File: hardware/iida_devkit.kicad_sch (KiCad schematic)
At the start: 7 parts

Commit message: HW: Refactor the schematics
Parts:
- added R101, R102: 0 Ω, Resistor_SMD:R_1206_3216Metric, symbol Device:R
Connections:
- net GND: now also R101.2, R102.2; no longer H101.1, H102.1, H103.1, H104.1
- new net CHASSIS: H101.1, H102.1, H103.1, H104.1, R101.1, R102.1
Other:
- removed sheet Battery
- removed sheet USB
- sheet Microcontroller ports: added I2C, USB; removed I2C_SCL, I2C_SDA, USB_DN, USB_DP
- sheet Power ports: added BAT_MON_INTn, I2C, USB; removed V_5V0, V_BAT
- note added: "2. Power"
- note added: "3. Microcontroller"
- note added: "Block diagram"
- note added: "Description"
- note added: "Mechanical"
- note added: "Notes"
- note added: "Table of Contents"
- note removed: "2. USB"
- note removed: "3. Battery"
- note removed: "4. Power"
- note removed: "5. Microcontroller"
- moved on the sheet: FID101, FID102, FID103, H101, H102, H103, H104

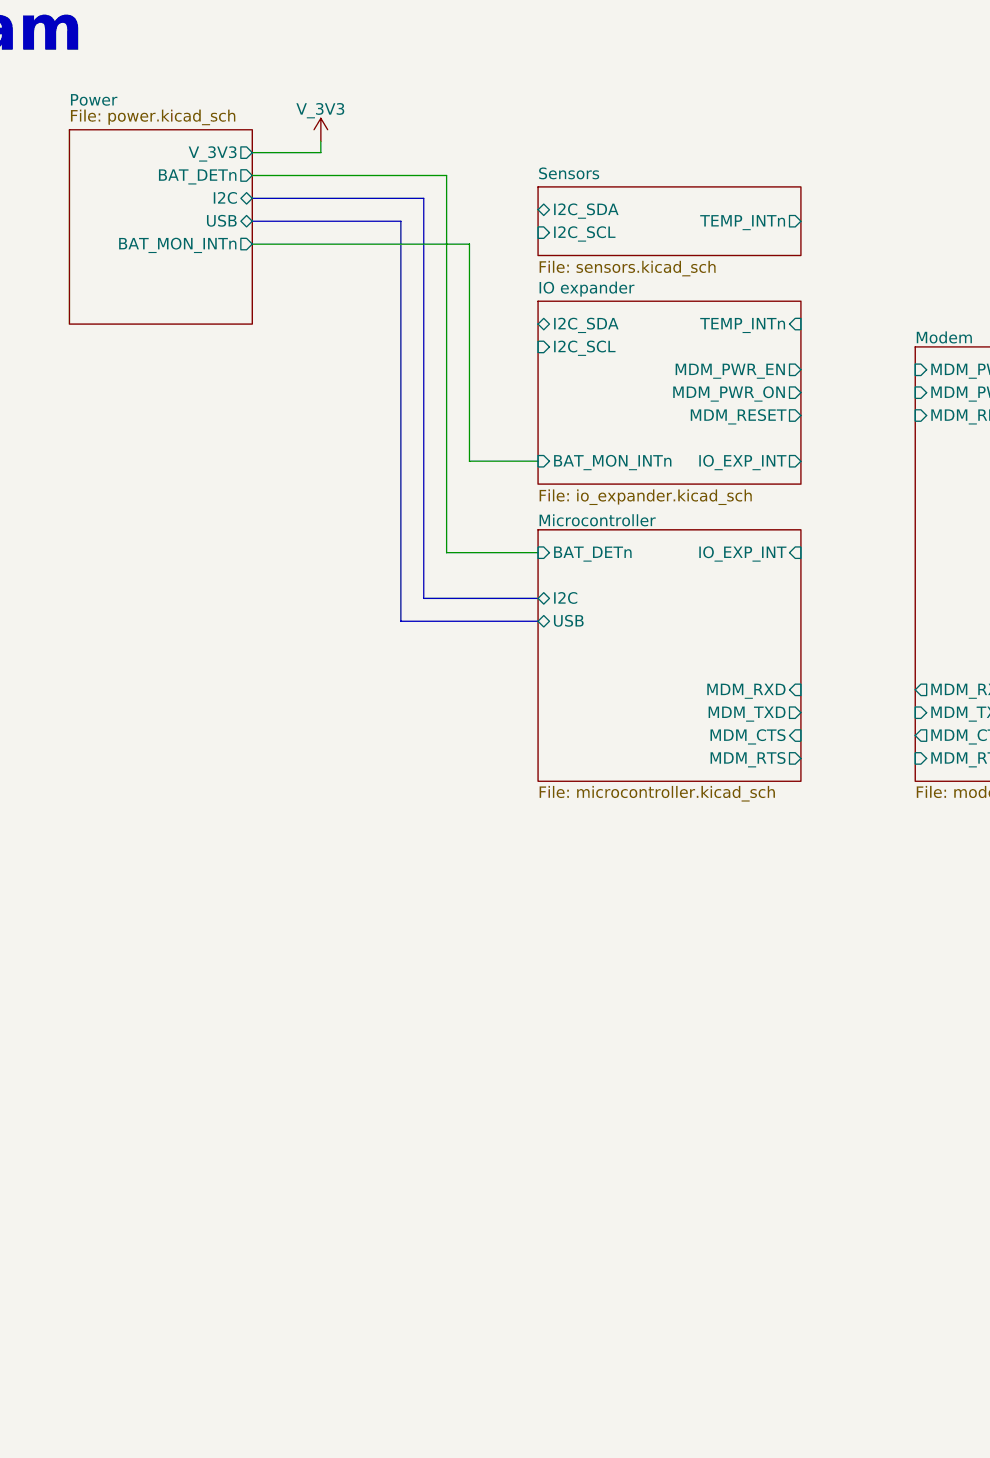
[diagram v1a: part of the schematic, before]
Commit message: Add EEPROM
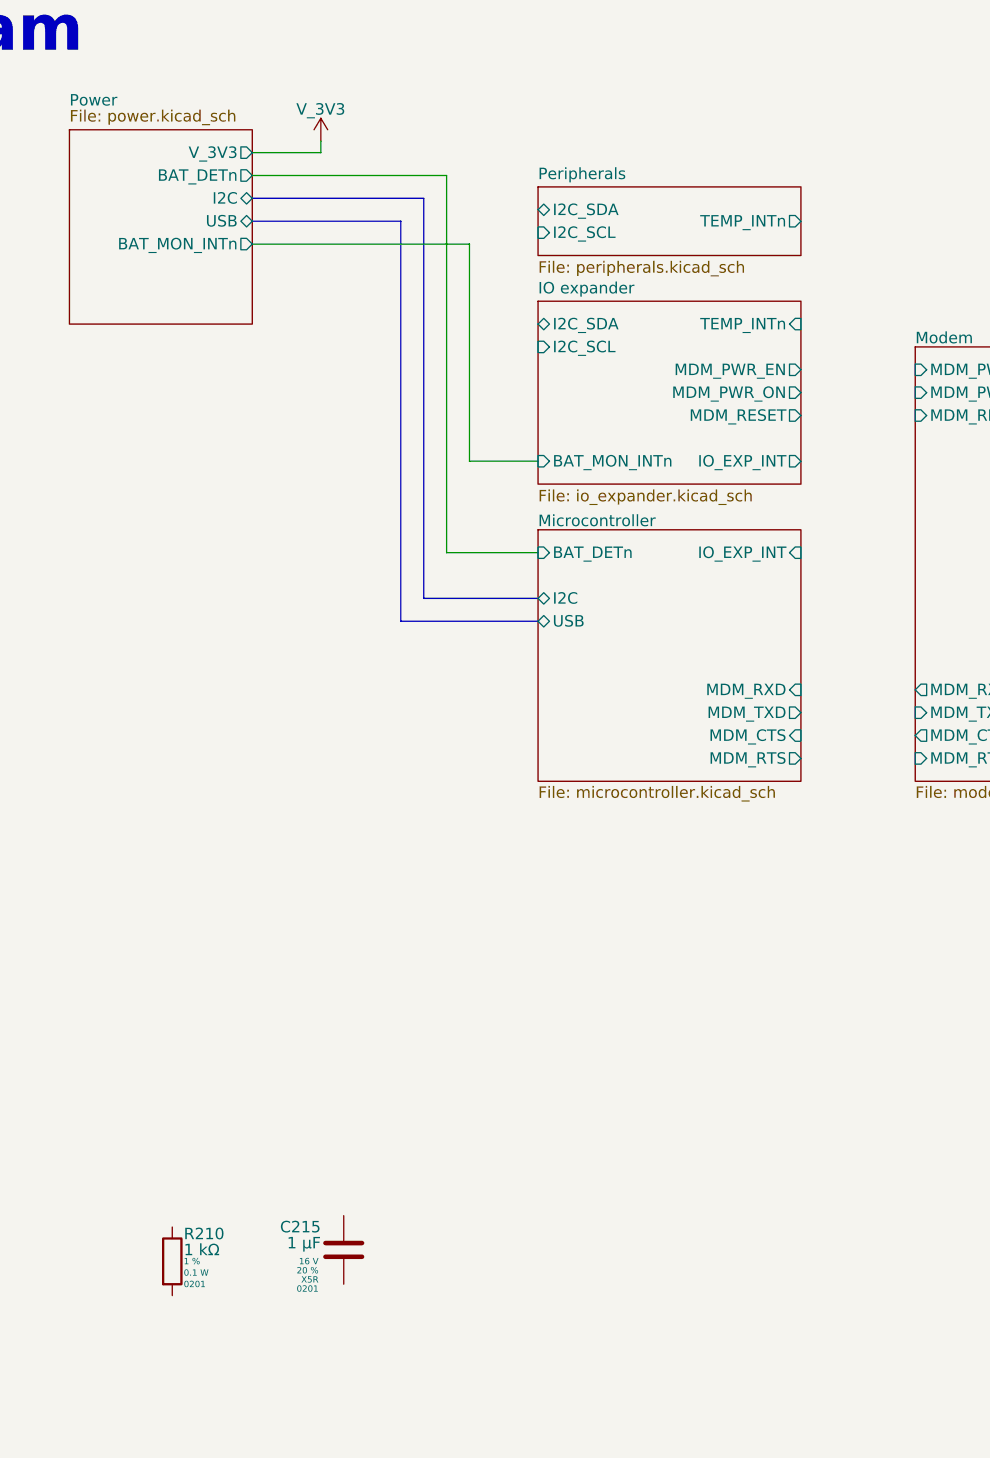
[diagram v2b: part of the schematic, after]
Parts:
- added C215: 1 µF, perfect_footprints:C_0201_0603Metric, symbol Device:C
- added R210: 1 kΩ, perfect_footprints:R_0201_0603Metric, symbol Device:R
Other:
- sheet Sensors renamed Peripherals
- sheet Peripherals: file sensors.kicad_sch -> peripherals.kicad_sch

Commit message: Refine schematics
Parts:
- removed C215: 1 µF, perfect_footprints:C_0201_0603Metric, symbol Device:C
- removed R210: 1 kΩ, perfect_footprints:R_0201_0603Metric, symbol Device:R
- renumbered FID101 to FID1, FID102 to FID2, FID103 to FID3, H101 to H1, H102 to H2, H103 to H3, H104 to H4, R102 to R1, R101 to R2
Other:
- removed sheet IO expander
- sheet Microcontroller ports: added EEPROM_WCn, {FLASH_QSPI}, {I2C}, {USB}; removed I2C, USB
- sheet Modem ports: added {SIM}; removed SIM_CLK, SIM_IO, SIM_RST
- sheet Peripherals ports: added BAT_MON_INTn, EEPROM_WCn, IO_EXP_INT, MDM_PWR_EN, MDM_PWR_ON, MDM_RESET, {FLASH_QSPI}, {I2C}; removed I2C_SCL, I2C_SDA, TEMP_INTn
- sheet Power ports: added {I2C}, {USB}; removed I2C, USB
- sheet SIM ports: added {SIM}; removed SIM_CLK, SIM_IO, SIM_RST
- note added: "4. Peripherals"
- note added: "5. Modem"
- note added: "6. SIM"
- note added: "7. Antennas"
- note removed: "10. Antennas"
- note removed: "6. Sensors"
- note removed: "7. IO expander"
- note removed: "8. Modem"
- note removed: "9. SIM"

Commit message: HW: Refine PDN
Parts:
- C1: renamed from R1; value 0 Ω -> 0.047 µF; footprint Resistor_SMD:R_1206_3216Metric -> Capacitor_SMD:C_1206_3216Metric; symbol Device:R -> Device:C; Digi-Key Part Number RMCF1206ZT0R00CT-ND -> (none); MPN RMCF1206ZT0R00 -> (none); Manufacturer Stackpole Electronics Inc -> (none); now not fitted; now left out of the parts list
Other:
- note added: "Place closely together."
- moved on the sheet: FID1, FID2, FID3, H1, H2, H3, H4, R2

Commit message: HW: Refine schematics
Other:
- sheet Microcontroller ports: added ST; removed BAT_DETn
- sheet Power ports: added ST; removed BAT_DETn
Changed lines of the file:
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@@
 			)
 		)
-		(pin "BAT_DETn" output
+		(pin "ST" output
 			(at 234.95 68.58 0)
 			(effects
@@
 			)
 		)
-		(pin "BAT_DETn" input
+		(pin "ST" input
 			(at 247.65 107.95 180)
 			(effects

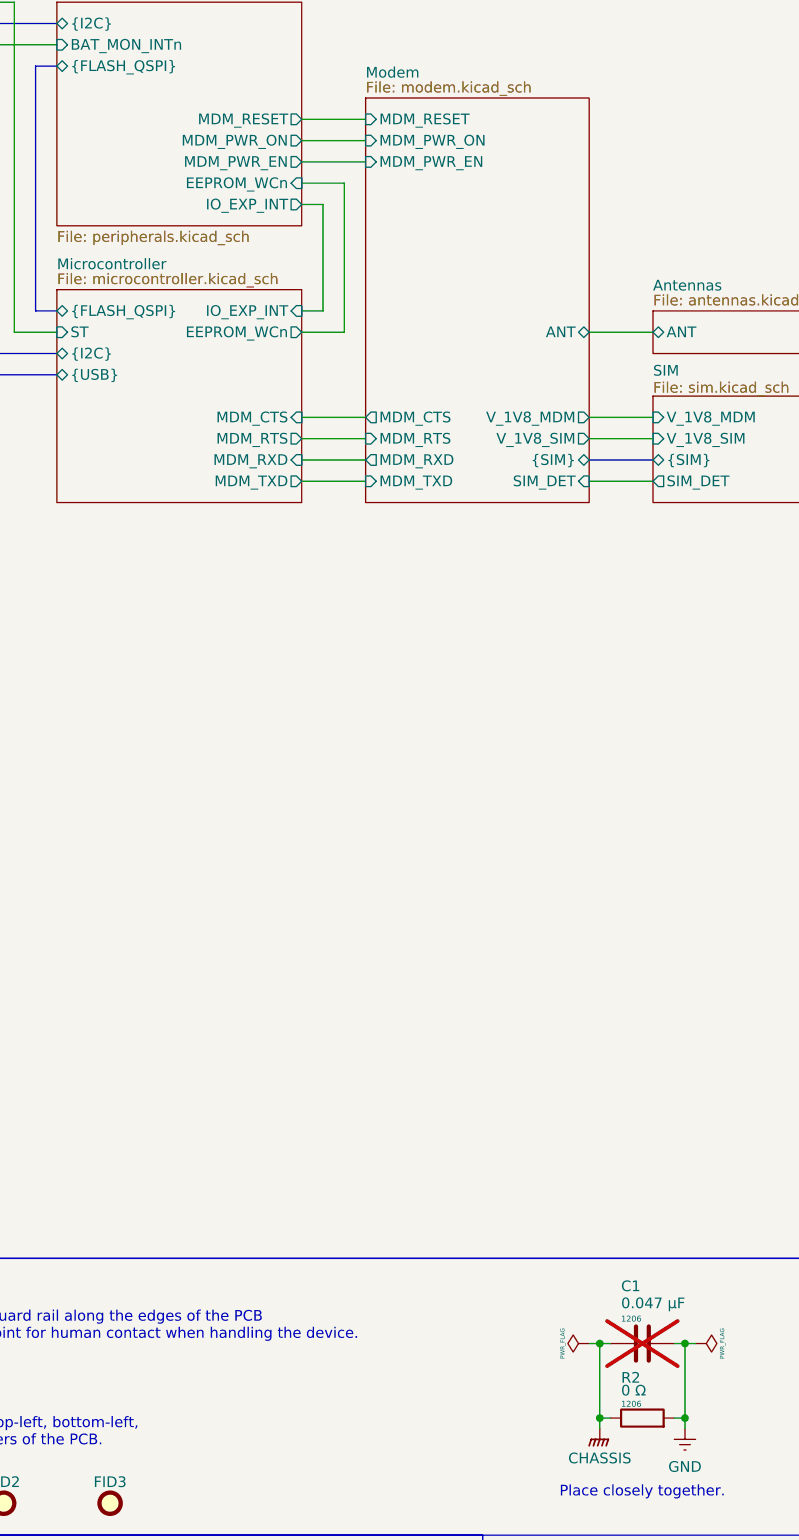
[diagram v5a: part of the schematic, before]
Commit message: HW: Redo MDM UART
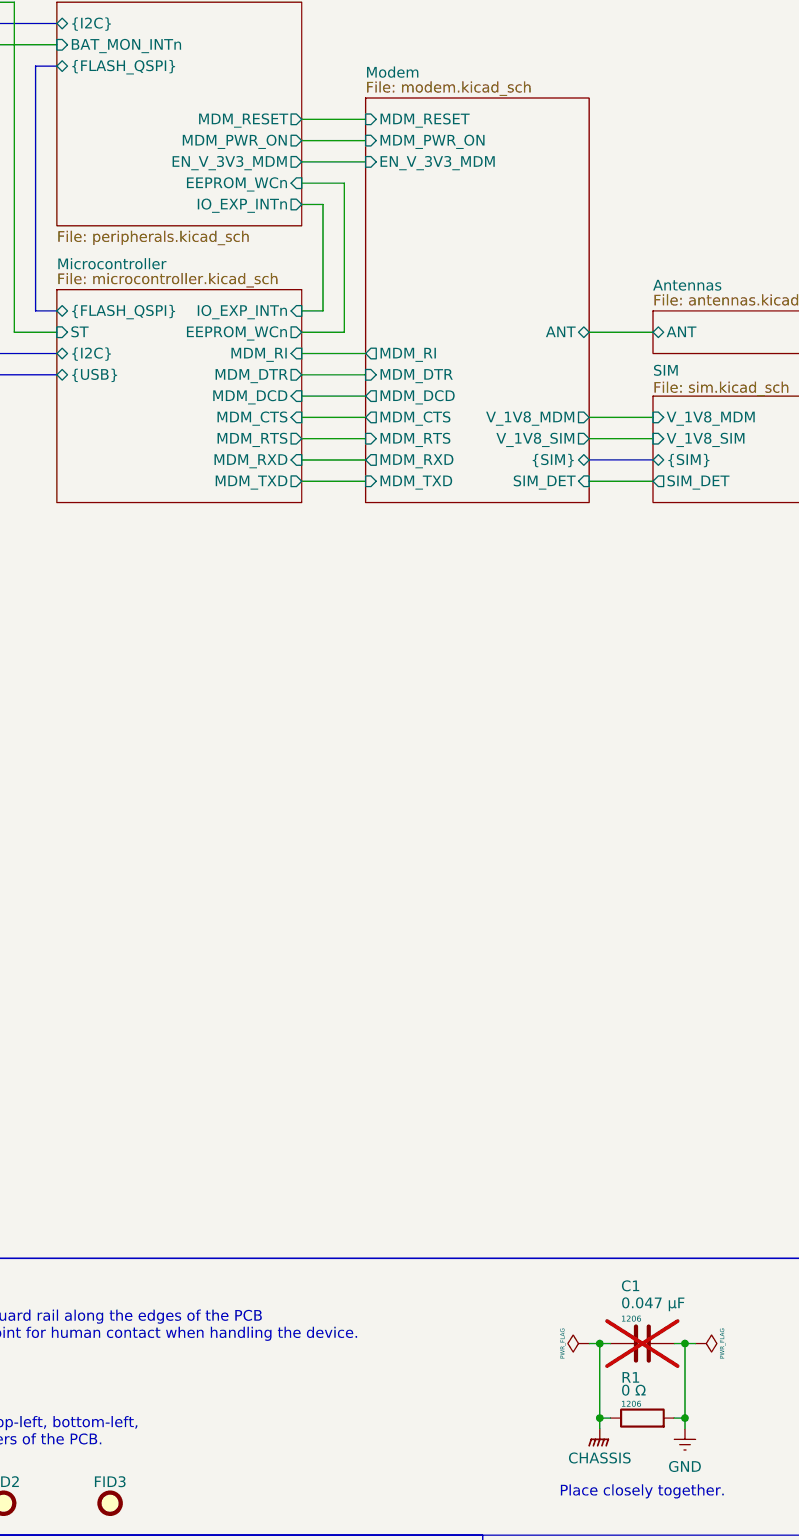
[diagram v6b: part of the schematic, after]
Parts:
- renumbered R2 to R1
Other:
- sheet Microcontroller ports: added IO_EXP_INTn, MDM_DCD, MDM_DTR, MDM_RI; removed IO_EXP_INT
- sheet Modem ports: added EN_V_3V3_MDM, MDM_DCD, MDM_DTR, MDM_RI; removed MDM_PWR_EN
- sheet Peripherals ports: added EN_V_3V3_MDM, IO_EXP_INTn; removed IO_EXP_INT, MDM_PWR_EN
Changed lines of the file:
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@@
+	(wire
+		(pts
+			(xy 276.86 110.49) (xy 284.48 110.49)
+		)
+		(stroke
+			(width 0)
+			(type default)
+		)
+	)
 	(wire
 		(pts
@@
 	(wire
 		(pts
+			(xy 276.86 115.57) (xy 284.48 115.57)
+		)
+		(stroke
+			(width 0)
+			(type default)
+		)
+	)
+	(wire
+		(pts
 			(xy 313.69 228.6) (xy 312.42 228.6)
 		)
@@
 		(pts
 			(xy 240.03 71.12) (xy 240.03 110.49)
+		)
+		(stroke
+			(width 0)
+			(type default)
+		)
+	)
+	(wire
+		(pts
+			(xy 276.86 113.03) (xy 284.48 113.03)
 		)
 		(stroke
@@
 		(in_pos_files yes)
 		(dnp no)
-		(property "Reference" "#PWR02"
+		(property "Reference" "#PWR04"
 			(at 322.58 245.11 0)
 			(hide yes)
@@
 			(project "iida_devkit"
 				(path "/b12a6e25-97fb-4aba-bc96-af8db389bb9a"
-					(reference "#PWR02")
+					(reference "#PWR04")
 					(unit 1)
 				)
@@
 		(in_pos_files yes)
 		(dnp no)
-		(property "Reference" "#PWR04"
+		(property "Reference" "#PWR02"
 			(at 242.57 68.58 0)
 			(hide yes)
@@
 			(project "iida_devkit"
 				(path "/b12a6e25-97fb-4aba-bc96-af8db389bb9a"
-					(reference "#PWR04")
+					(reference "#PWR02")
 					(unit 1)
 				)
@@
 		(in_pos_files yes)
 		(dnp no)
-		(property "Reference" "#PWR03"
+		(property "Reference" "#PWR01"
 			(at 187.96 250.19 0)
 			(hide yes)
@@
 			(project "iida_devkit"
 				(path "/b12a6e25-97fb-4aba-bc96-af8db389bb9a"
-					(reference "#PWR03")
+					(reference "#PWR01")
 					(unit 1)
 				)
@@
 		(in_pos_files yes)
 		(dnp no)
-		(property "Reference" "#PWR01"
+		(property "Reference" "#PWR03"
 			(at 312.42 243.84 0)
 			(hide yes)
@@
 			(project "iida_devkit"
 				(path "/b12a6e25-97fb-4aba-bc96-af8db389bb9a"
-					(reference "#PWR01")
+					(reference "#PWR03")
 					(unit 1)
 				)
@@
 		(in_pos_files yes)
 		(dnp no)
-		(property "Reference" "R2"
+		(property "Reference" "R1"
 			(at 314.96 233.426 90)
 			(show_name no)
@@
 			(project "iida_devkit"
 				(path "/b12a6e25-97fb-4aba-bc96-af8db389bb9a"
-					(reference "R2")
+					(reference "R1")
 					(unit 1)
 				)
@@
 			)
 		)
-		(pin "MDM_PWR_EN" input
-			(at 284.48 87.63 180)
-			(effects
-				(font
-					(size 1.27 1.27)
-				)
-				(justify left)
-			)
-		)
 		(pin "MDM_PWR_ON" input
 			(at 284.48 85.09 180)
@@
 				)
 				(justify right)
+			)
+		)
+		(pin "EN_V_3V3_MDM" input
+			(at 284.48 87.63 180)
+			(effects
+				(font
+					(size 1.27 1.27)
+				)
+				(justify left)
+			)
+		)
+		(pin "MDM_DCD" output
+			(at 284.48 115.57 180)
+			(effects
+				(font
+					(size 1.27 1.27)
+				)
+				(justify left)
+			)
+		)
+		(pin "MDM_DTR" input
+			(at 284.48 113.03 180)
+			(effects
+				(font
+					(size 1.27 1.27)
+				)
+				(justify left)
+			)
+		)
+		(pin "MDM_RI" output
+			(at 284.48 110.49 180)
+			(effects
+				(font
+					(size 1.27 1.27)
+				)
+				(justify left)
 			)
 		)
@@
 			)
 		)
-		(pin "IO_EXP_INT" input
+		(pin "IO_EXP_INTn" input
 			(at 276.86 105.41 0)
 			(effects
@@
 				)
 				(justify left)
+			)
+		)
+		(pin "MDM_DCD" input
+			(at 276.86 115.57 0)
+			(effects
+				(font
+					(size 1.27 1.27)
+				)
+				(justify right)
+			)
+		)
+		(pin "MDM_DTR" output
+			(at 276.86 113.03 0)
+			(effects
+				(font
+					(size 1.27 1.27)
+				)
+				(justify right)
+			)
+		)
+		(pin "MDM_RI" input
+			(at 276.86 110.49 0)
+			(effects
+				(font
+					(size 1.27 1.27)
+				)
+				(justify right)
 			)
 		)
@@
 			)
 		)
-		(pin "IO_EXP_INT" output
+		(pin "IO_EXP_INTn" output
 			(at 276.86 92.71 0)
 			(effects
@@
 			)
 		)
-		(pin "MDM_PWR_EN" output
+		(pin "EN_V_3V3_MDM" output
 			(at 276.86 87.63 0)
 			(effects
